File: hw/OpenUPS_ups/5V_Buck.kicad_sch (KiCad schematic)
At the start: 24 parts, among them U201 TPS51397A, U202 INA180A3

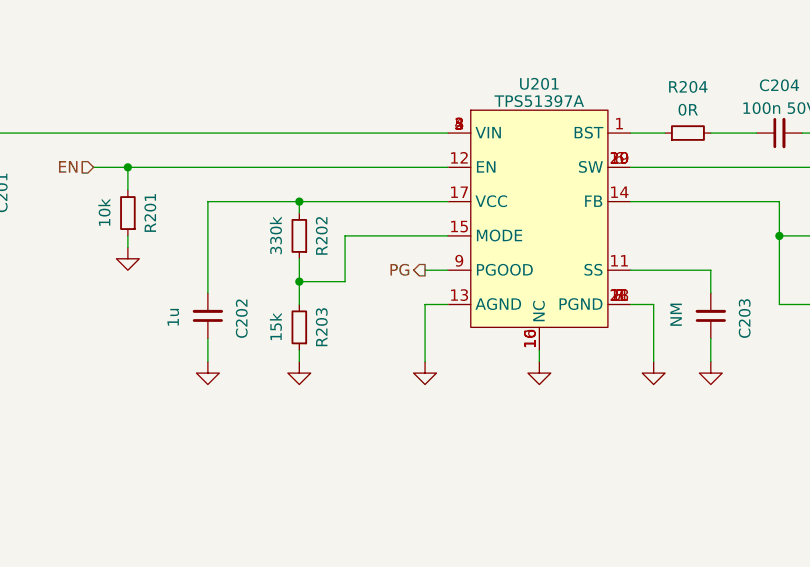
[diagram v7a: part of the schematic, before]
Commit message: BMS placement complete (no routing)
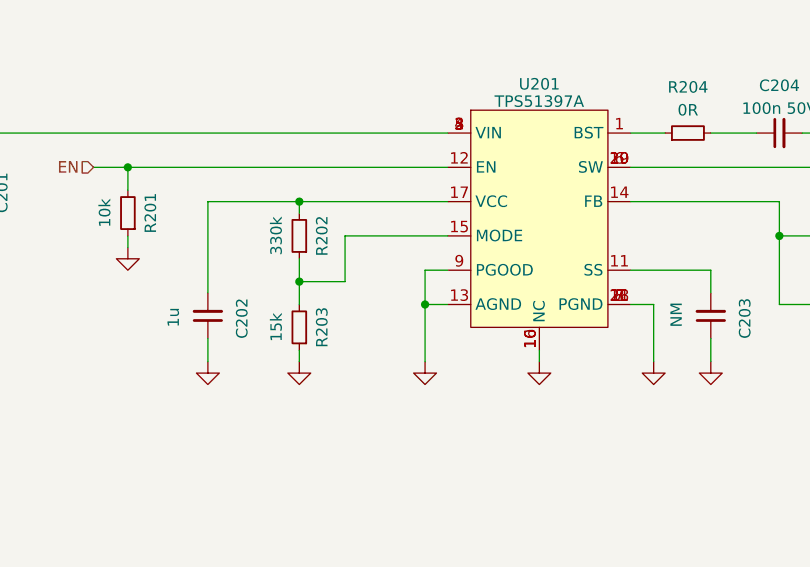
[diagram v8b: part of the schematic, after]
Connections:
- net PG is gone; now on net GND: U201.9 (PGOOD)
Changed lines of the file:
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@@
   (junction (at 184.15 71.12) (diameter 0) (color 0 0 0 0)
   )
+  (junction (at 118.11 78.74) (diameter 0) (color 0 0 0 0)
+  )
   (junction (at 219.71 80.01) (diameter 0) (color 0 0 0 0)
   )
@@
   )
   (wire (pts (xy 163.83 59.69) (xy 160.02 59.69))
+    (stroke (width 0) (type default))
+  )
+  (wire (pts (xy 118.11 74.93) (xy 118.11 78.74))
     (stroke (width 0) (type default))
   )
@@
     (effects (font (size 1.27 1.27)) (justify right))
   )
-  (hierarchical_label "PG" (shape output) (at 118.11 74.93 180) (fields_autoplaced)
-    (effects (font (size 1.27 1.27)) (justify right))
-  )
